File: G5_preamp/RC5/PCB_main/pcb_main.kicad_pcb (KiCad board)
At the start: 2 copper layers, 165 x 60 mm, 52 parts, among them J1 PSU_TUBE, J2 PCB_TUBE, J3 PSU_AMP, J4 AMP, J5 PSU_SIMCAB, J6 SIMCAB, J7 3PDT, J8 PCB_OUTPUT, Q1 MPS751, Q2 IRF740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

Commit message: update pcb_main tracks
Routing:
- net GNDS: track 471.2 -> 467.4 mm
- net /OUT_JACK: track 113.4 -> 110.9 mm
- net /NFB: track 61.1 -> 61.7 mm
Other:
- board text added: "2019 - RC5"
- board text removed: "2019 - RC4"

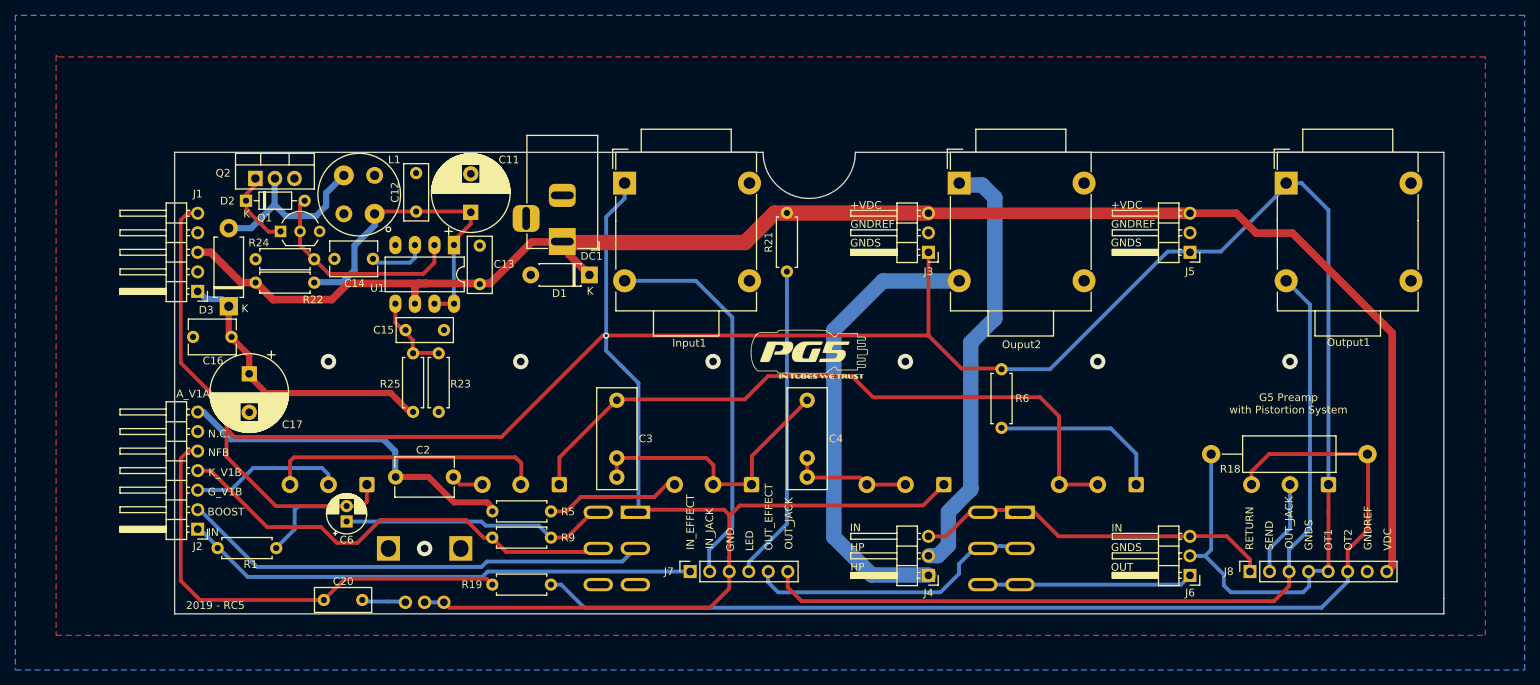
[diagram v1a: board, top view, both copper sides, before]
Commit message: Cosmetic_update_pcb
R6 move
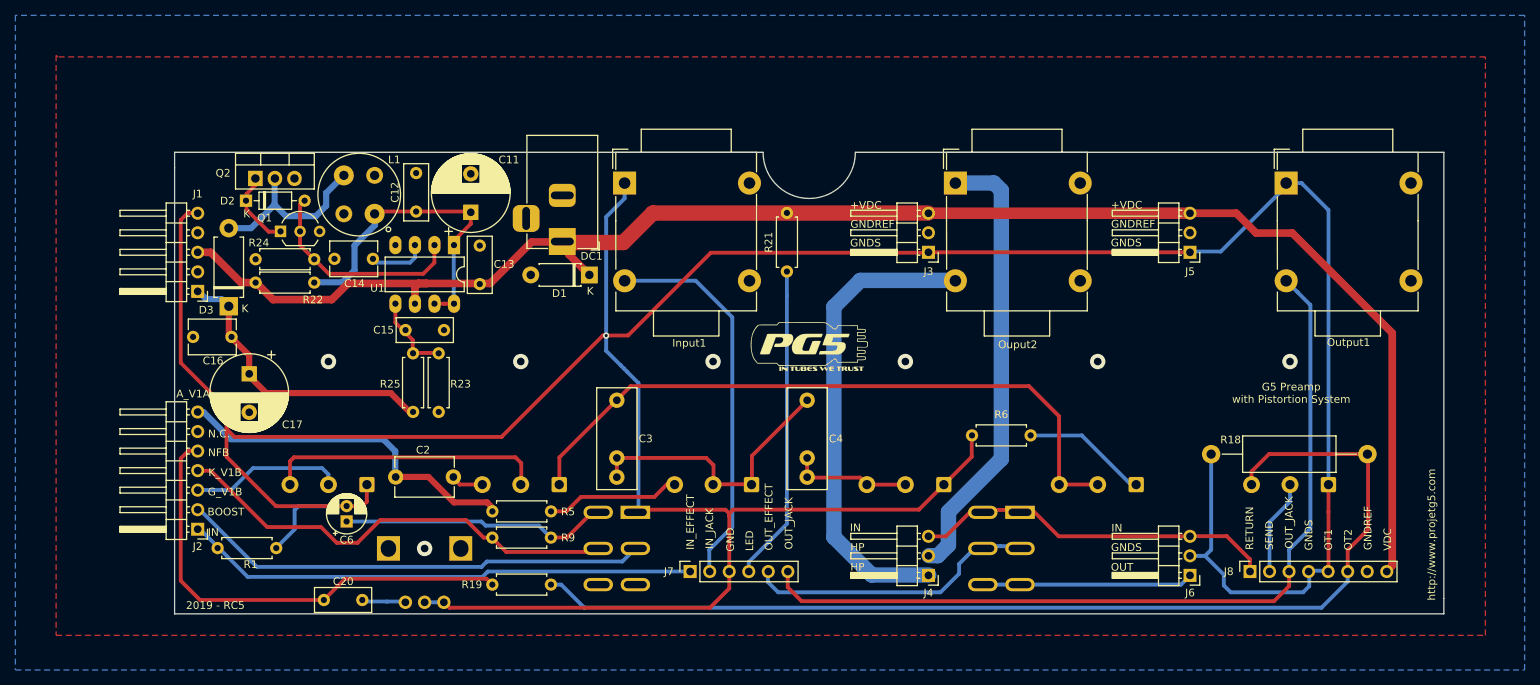
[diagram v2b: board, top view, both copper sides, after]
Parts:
- moved R6 3.90 mm to (191.3, 138.8), turned to 180 degrees
- moved U2 1.00 mm to (162.5, 127.0)
- moved Ouput2 0.50 mm to (181.5, 118.7)
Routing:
- net GNDS: track 467.4 -> 461.8 mm
- net Net-(Bass1-Pad1): track 21.9 -> 16.3 mm
- net /HP2: track 56.2 -> 58.5 mm
- net /HP1: track 60.2 -> 61.5 mm
- net Net-(Bass1-Pad2): track 88.9 -> 87.8 mm
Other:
- board text added: "http://www.projetg5.com"
